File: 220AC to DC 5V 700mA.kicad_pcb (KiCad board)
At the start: 2 copper layers, 22 parts, among them IC1 HF2812H, T1 Transformer_1P_2S

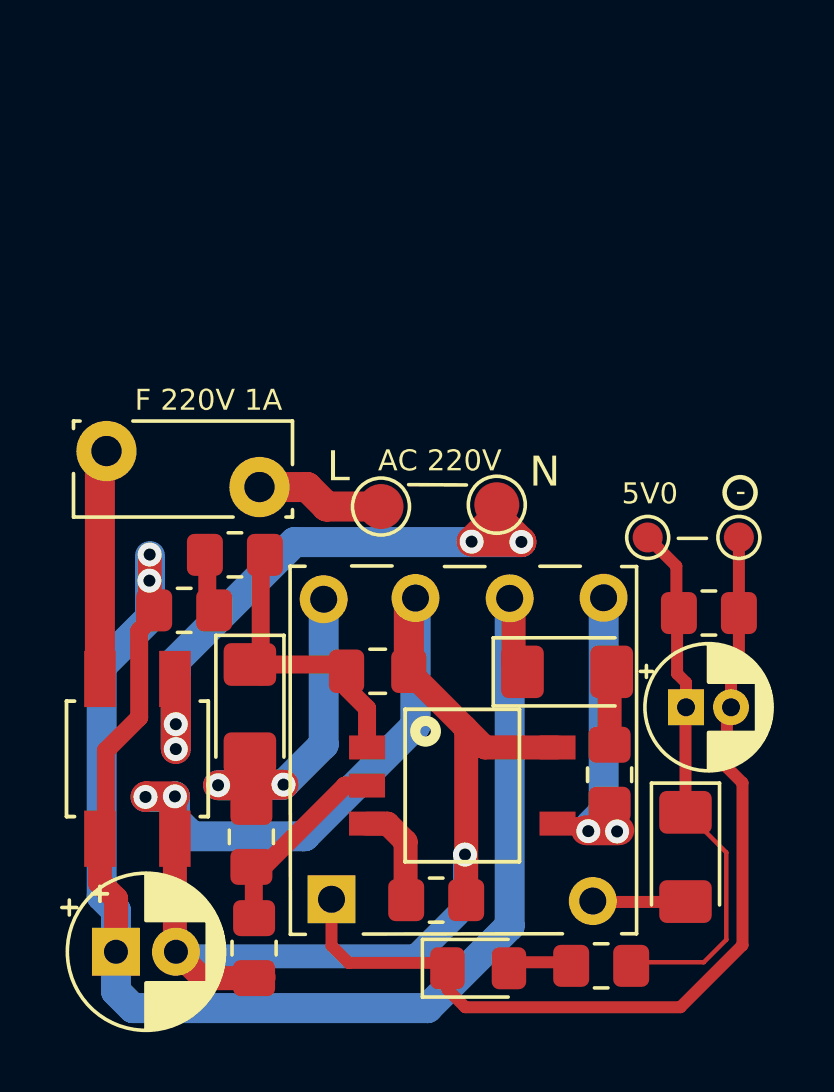
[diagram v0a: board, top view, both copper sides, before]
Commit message: rev. update
bug track correction ; added overcurrent protection
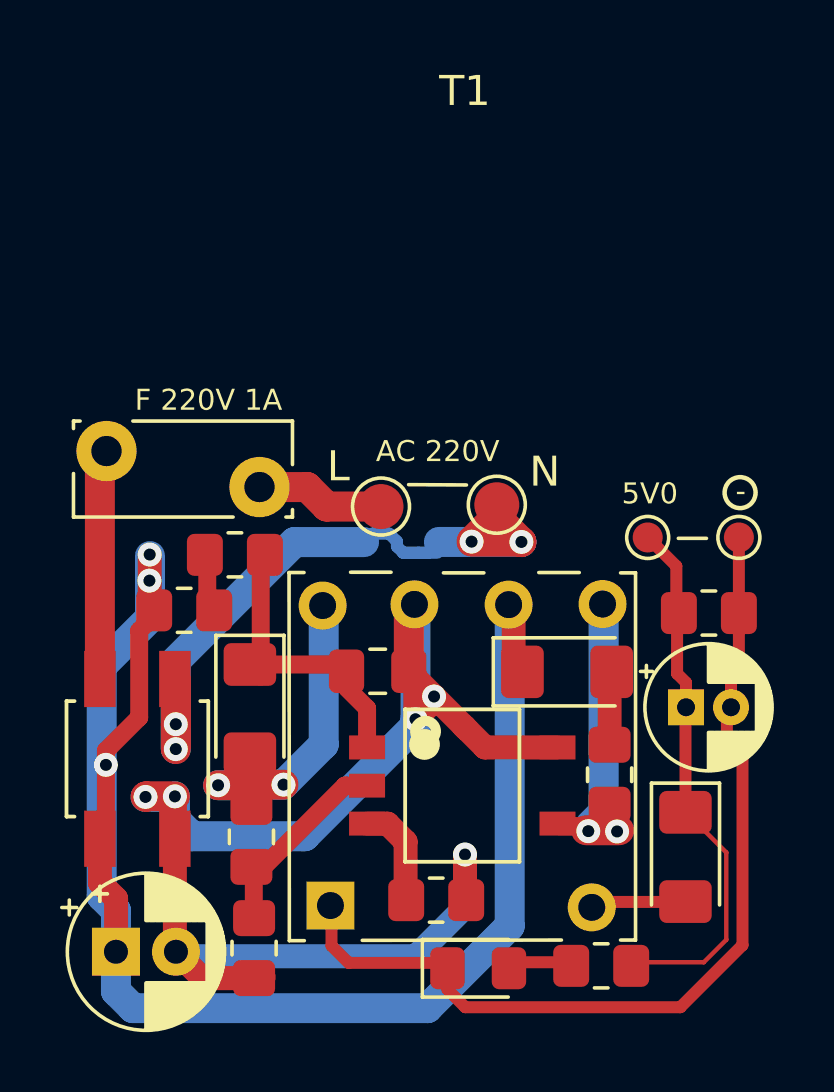
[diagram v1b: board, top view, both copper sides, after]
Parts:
- removed REF**: Symbol_Highvoltage_Type2_Front_Silk_Small, Symbol:Symbol_Highvoltage_Type2_Front_Silk_Small
- moved T1 0.21 mm to (136.0, 94.6)
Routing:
- net Net-(AC220V_IN1-Pad2): track 22.8 -> 24.6 mm
- net Net-(12K7-Pad2): track 54.2 -> 52.7 mm, vias 1 -> 3
- net Net-(4M7-Pad2): vias 0 -> 1
